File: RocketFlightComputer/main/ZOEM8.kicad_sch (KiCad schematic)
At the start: 7 parts, among them Y4 32.768kHz

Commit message: Addition of all components in BOM, metal mounting plates, need to check psram if its ok for signals to pass under, all components need a double check
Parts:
- C38: value 4.7UF -> 4.7uF; LCSC (none) -> C19666
- C39: value 0.1UF -> 0.1uF; LCSC (none) -> C48579250
- CONMHF1-SMD-G-T1: LCSC (none) -> C22442695
- D7: renamed from D5; LCSC (none) -> C233388
- L3: renamed from L5; value 2.2μ -> 2.2μH; footprint ZOE-M8Q:0806 -> Inductor_SMD:L_0805_2012Metric_Pad1.05x1.20mm_HandSolder; LCSC (none) -> C83998; Mouser Part Number (none) -> 81-LQM2MPN2R2NG0L
- U-BLOX_ZOE_M8Q-0-1: renamed from U-BLOX_ZOE_M8Q-0-10; LCSC (none) -> C7398634; Mouser Part Number (none) -> 377-ZOE-M8Q-0
- Y4: LCSC (none) -> C7462219; Mouser Part Number (none) -> 428-202816-MC01
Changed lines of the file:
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@@
+			)
+		)
+		(property "LCSC" "C7462219"
+			(at 240.03 119.38 0)
+			(effects
+				(font
+					(size 1.27 1.27)
+				)
+				(hide yes)
+			)
+		)
+		(property "Mouser Part Number" "428-202816-MC01"
+			(at 240.03 119.38 0)
+			(effects
+				(font
+					(size 1.27 1.27)
+				)
+				(hide yes)
 			)
 		)
@@
 		(dnp no)
 		(fields_autoplaced yes)
-		(property "Reference" "#PWR0157"
+		(property "Reference" "#PWR0104"
 			(at 74.93 171.45 0)
 			(effects
@@
 			(project "main"
 				(path "/27195d1d-92b2-40df-ada5-3b20841577e7/29f0379a-3100-4813-a2e2-86f2e88b3e64"
-					(reference "#PWR0157")
+					(reference "#PWR0104")
 					(unit 1)
 				)
@@
 		(on_board yes)
 		(dnp no)
-		(property "Reference" "U-BLOX_ZOE_M8Q-0-10"
+		(property "Reference" "U-BLOX_ZOE_M8Q-0-1"
 			(at 179.07 97.79 0)
 			(effects
@@
 			)
 		)
+		(property "Mouser Part Number" "377-ZOE-M8Q-0"
+			(at 194.31 125.73 0)
+			(effects
+				(font
+					(size 1.27 1.27)
+				)
+				(hide yes)
+			)
+		)
+		(property "LCSC" "C7398634"
+			(at 194.31 125.73 0)
+			(effects
+				(font
+					(size 1.27 1.27)
+				)
+				(hide yes)
+			)
+		)
 		(pin "1"
 		)
@@
 			(project "main"
 				(path "/27195d1d-92b2-40df-ada5-3b20841577e7/29f0379a-3100-4813-a2e2-86f2e88b3e64"
-					(reference "U-BLOX_ZOE_M8Q-0-10")
+					(reference "U-BLOX_ZOE_M8Q-0-1")
 					(unit 1)
 				)
@@
 		(dnp no)
 		(fields_autoplaced yes)
-		(property "Reference" "#PWR0101"
+		(property "Reference" "#PWR0108"
 			(at 218.44 140.97 0)
 			(effects
@@
 			(project "main"
 				(path "/27195d1d-92b2-40df-ada5-3b20841577e7/29f0379a-3100-4813-a2e2-86f2e88b3e64"
-					(reference "#PWR0101")
+					(reference "#PWR0108")
 					(unit 1)
 				)
@@
 		(on_board yes)
 		(dnp no)
-		(property "Reference" "#FLG05"
+		(property "Reference" "#FLG03"
 			(at 168.91 106.045 0)
 			(effects
@@
 			(project ""
 				(path "/27195d1d-92b2-40df-ada5-3b20841577e7/29f0379a-3100-4813-a2e2-86f2e88b3e64"
-					(reference "#FLG05")
+					(reference "#FLG03")
 					(unit 1)
 				)
@@
 		(on_board yes)
 		(dnp no)
-		(property "Reference" "#FLG06"
+		(property "Reference" "#FLG04"
 			(at 173.99 112.395 0)
 			(effects
@@
 			(project "main"
 				(path "/27195d1d-92b2-40df-ada5-3b20841577e7/29f0379a-3100-4813-a2e2-86f2e88b3e64"
-					(reference "#FLG06")
+					(reference "#FLG04")
 					(unit 1)
 				)
@@
 				)
 				(justify left top)
+				(hide yes)
+			)
+		)
+		(property "LCSC" "C22442695 "
+			(at 38.1 171.45 0)
+			(effects
+				(font
+					(size 1.27 1.27)
+				)
 				(hide yes)
 			)
@@
 		(dnp no)
 		(fields_autoplaced yes)
-		(property "Reference" "#PWR0155"
+		(property "Reference" "#PWR0103"
 			(at 53.34 195.58 0)
 			(effects
@@
 			(project "main"
 				(path "/27195d1d-92b2-40df-ada5-3b20841577e7/29f0379a-3100-4813-a2e2-86f2e88b3e64"
-					(reference "#PWR0155")
+					(reference "#PWR0103")
 					(unit 1)
 				)
@@
 		(on_board yes)
 		(dnp no)
-		(property "Reference" "#PWR0152"
+		(property "Reference" "#PWR0106"
 			(at 161.29 102.87 0)
 			(effects
@@
 			(project "main"
 				(path "/27195d1d-92b2-40df-ada5-3b20841577e7/29f0379a-3100-4813-a2e2-86f2e88b3e64"
-					(reference "#PWR0152")
+					(reference "#PWR0106")
 					(unit 1)
 				)
@@
 		(dnp no)
 		(fields_autoplaced yes)
-		(property "Reference" "#PWR098"
+		(property "Reference" "#PWR0105"
 			(at 156.845 154.94 0)
 			(effects
@@
 			(project "main"
 				(path "/27195d1d-92b2-40df-ada5-3b20841577e7/29f0379a-3100-4813-a2e2-86f2e88b3e64"
-					(reference "#PWR098")
+					(reference "#PWR0105")
 					(unit 1)
 				)
@@
 			)
 		)
-		(property "Value" "4.7UF"
+		(property "Value" "4.7uF"
 			(at 147.574 126.746 0)
 			(effects
@@
 		)
 		(property "Description" "X5R 4U7 10% 6.3 V"
+			(at 156.845 123.19 0)
+			(effects
+				(font
+					(size 1.27 1.27)
+				)
+				(hide yes)
+			)
+		)
+		(property "LCSC" "C19666 "
 			(at 156.845 123.19 0)
 			(effects
@@
 		(dnp no)
 		(fields_autoplaced yes)
-		(property "Reference" "#PWR0100"
+		(property "Reference" "#PWR0107"
 			(at 172.085 154.94 0)
 			(effects
@@
 			(project "main"
 				(path "/27195d1d-92b2-40df-ada5-3b20841577e7/29f0379a-3100-4813-a2e2-86f2e88b3e64"
-					(reference "#PWR0100")
+					(reference "#PWR0107")
 					(unit 1)
 				)
@@
 		(dnp no)
 		(fields_autoplaced yes)
-		(property "Reference" "D5"
+		(property "Reference" "D7"
 			(at 57.15 143.5099 90)
 			(effects
@@
 			)
 		)
+		(property "LCSC" "C233388 "
+			(at 53.34 137.16 0)
+			(effects
+				(font
+					(size 1.27 1.27)
+				)
+				(hide yes)
+			)
+		)
 		(pin "2"
 		)
@@
 			(project "main"
 				(path "/27195d1d-92b2-40df-ada5-3b20841577e7/29f0379a-3100-4813-a2e2-86f2e88b3e64"
-					(reference "D5")
+					(reference "D7")
 					(unit 1)
 				)
@@
 		(dnp no)
 		(fields_autoplaced yes)
-		(property "Reference" "#PWR0156"
+		(property "Reference" "#PWR0102"
 			(at 31.75 171.45 0)
 			(effects
@@
 			(project "main"
 				(path "/27195d1d-92b2-40df-ada5-3b20841577e7/29f0379a-3100-4813-a2e2-86f2e88b3e64"
-					(reference "#PWR0156")
+					(reference "#PWR0102")
 					(unit 1)
 				)
@@
 			)
 		)
-		(property "Value" "0.1UF"
+		(property "Value" "0.1uF"
 			(at 180.848 133.858 0)
 			(effects
@@
 		)
 		(property "Description" ""
+			(at 172.085 130.81 0)
+			(effects
+				(font
+					(size 1.27 1.27)
+				)
+				(hide yes)
+			)
+		)
+		(property "LCSC" "C48579250"
 			(at 172.085 130.81 0)
 			(effects
@@
 		(on_board yes)
 		(dnp no)
-		(property "Reference" "L5"
+		(property "Reference" "L3"
 			(at 165.227 111.506 90)
 			(effects
@@
 			)
 		)
-		(property "Value" "2.2μ"
+		(property "Value" "2.2μH"
 			(at 167.894 116.332 90)
 			(effects
@@
 			)
 		)
-		(property "Footprint" "ZOE-M8Q:0806"
+		(property "Footprint" "Inductor_SMD:L_0805_2012Metric_Pad1.05x1.20mm_HandSolder"
 			(at 164.465 110.49 0)
 			(effects
@@
 			)
 		)
+		(property "LCSC" "C83998"
+			(at 164.465 110.49 0)
+			(effects
+				(font
+					(size 1.27 1.27)
+				)
+				(hide yes)
+			)
+		)
+		(property "Mouser Part Number" "81-LQM2MPN2R2NG0L"
+			(at 164.465 110.49 0)
+			(effects
+				(font
+					(size 1.27 1.27)
+				)
+				(hide yes)
+			)
+		)
 		(pin "1"
 		)
@@
 			(project "main"
 				(path "/27195d1d-92b2-40df-ada5-3b20841577e7/29f0379a-3100-4813-a2e2-86f2e88b3e64"
-					(reference "L5")
-					(unit 1)
-				)
+					(reference "L3")
+					(unit 1)
+				)

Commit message: Corrected a few subsystems
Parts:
- removed C38: 4.7uF, Resistor_SMD:R_0603_1608Metric_Pad0.98x0.95mm_HandSolder, symbol SparkFun_ZOE-M8Q GPS-eagle-import:4.7UF-0603-6.3V-(10%)
- removed D7: ESD9R3.3ST5G, footprint:ESD9R3_3ST5G, symbol ESD9R3_3ST5G:ESD9R3.3ST5G
- removed L3: 2.2μH, Inductor_SMD:L_0805_2012Metric_Pad1.05x1.20mm_HandSolder, symbol SparkFun_ZOE-M8Q GPS-eagle-import:2.2μH_SHIELDED_INDUCTOR
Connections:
- net +3.3V: now also U-BLOX_ZOE_M8Q-0-1.26 (V_DCDC_OUT), U-BLOX_ZOE_M8Q-0-1.27 (V_CORE)
- net ANT: now also CONMHF1-SMD-G-T1.1 (SIGNAL)
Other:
- moved on the sheet: C39, Y4

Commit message: Corrections of mistake, revision of schematic is done and BOM revised, revision of pcb layout to do
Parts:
- C39: LCSC C48579250 -> C1590
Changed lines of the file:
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@@
 			)
 		)
-		(property "LCSC" "C48579250"
+		(property "LCSC" "C1590"
 			(at 121.92 77.47 0)
 			(hide yes)

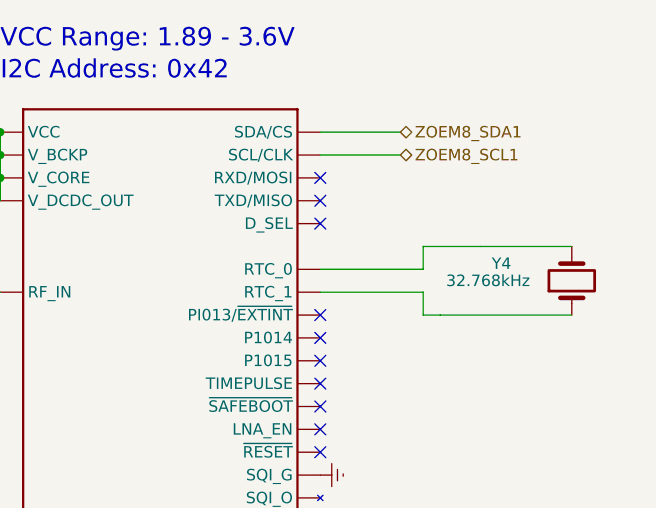
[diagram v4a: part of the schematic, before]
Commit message: Was missing pull ups on adxl375
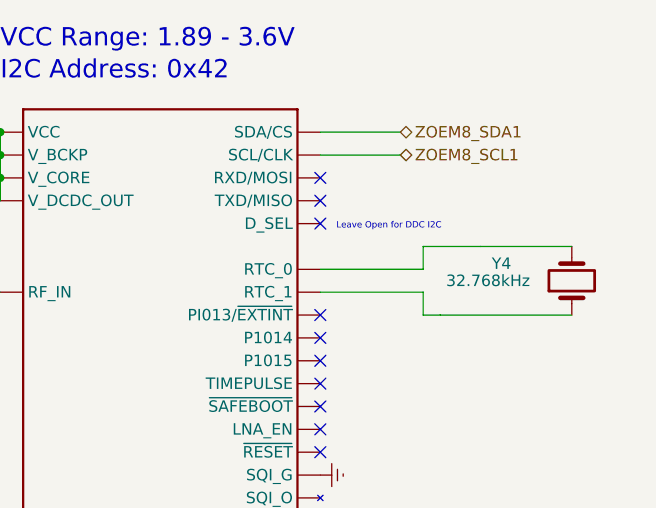
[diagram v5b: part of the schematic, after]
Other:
- note added: "Leave Open for DDC I2C"
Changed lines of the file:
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@@
+		)
+	)
+	(text "Leave Open for DDC I2C"
+		(exclude_from_sim no)
+		(at 171.958 82.042 0)
+		(effects
+			(font
+				(size 0.7 0.7)
+			)
+			(justify left bottom)
 		)
 	)
